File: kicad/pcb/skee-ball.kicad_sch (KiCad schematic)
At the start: 79 parts, among them J1 SPEAKER_P, J10 NHD_RW, J11 NHD_DB1, J12 NHD_DB0, J13 US_ECHO0, J14 US_ECHO1, J15 US_ECHO2, J16 US_ECHO3, J17 US_ECHO4, J18 US_TRIG0_5, J19 US_TRIG1_5, J2 SPEAKER_N, J20 US_TRIG2_5, J21 US_TRIG3_5, J22 US_TRIG4_5, J23 NHD_E1, J24 NHD_E2, J25 ADC_IN1, J26 PWM_SERVO_6, J27 PWM_DC (TIM17_CH1), J28 +24V, J29 NHD_V0, J3 NHD_DB7, J30 BUTTON_P, J31 BUTTON_N, J32 GND, J33 HEADER_GND, J34 HEADER_SWDIO, J35 HEADER_SWCLK, J4 NHD_DB6, J5 NHD_DB5, J6 NHD_DB4, J7 NHD_DB3, J8 NHD_DB2, J9 NHD_RS, U1 D24V22F6, U10 LD1117S33TR_SOT223, U11 LD1117S33TR_SOT223, U12 LD1117S33TR_SOT223, U13 LD1117S33TR_SOT223, U14 LD1117S33TR_SOT223, U2 MAX98357A, U3 D24V22F5, U4 STM32F091RCTx, U5 74HC595, U6 74HC595, U7 74LS08, U8 LD1117S33TR_SOT223, U9 LD1117S33TR_SOT223

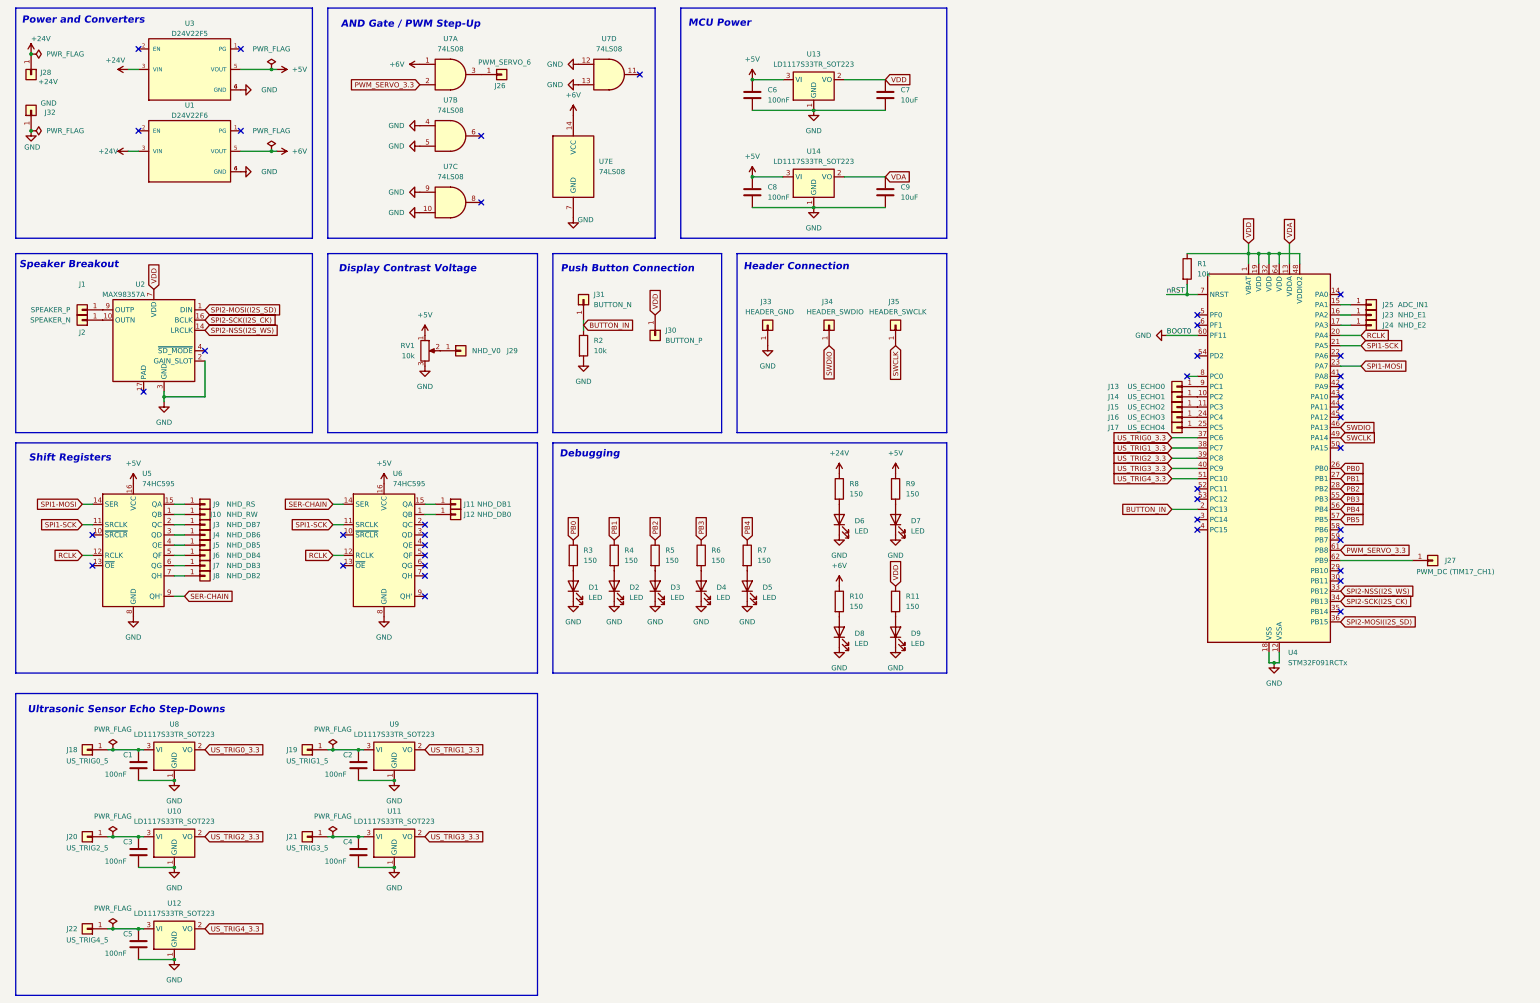
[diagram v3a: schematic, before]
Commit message: added pcb layout
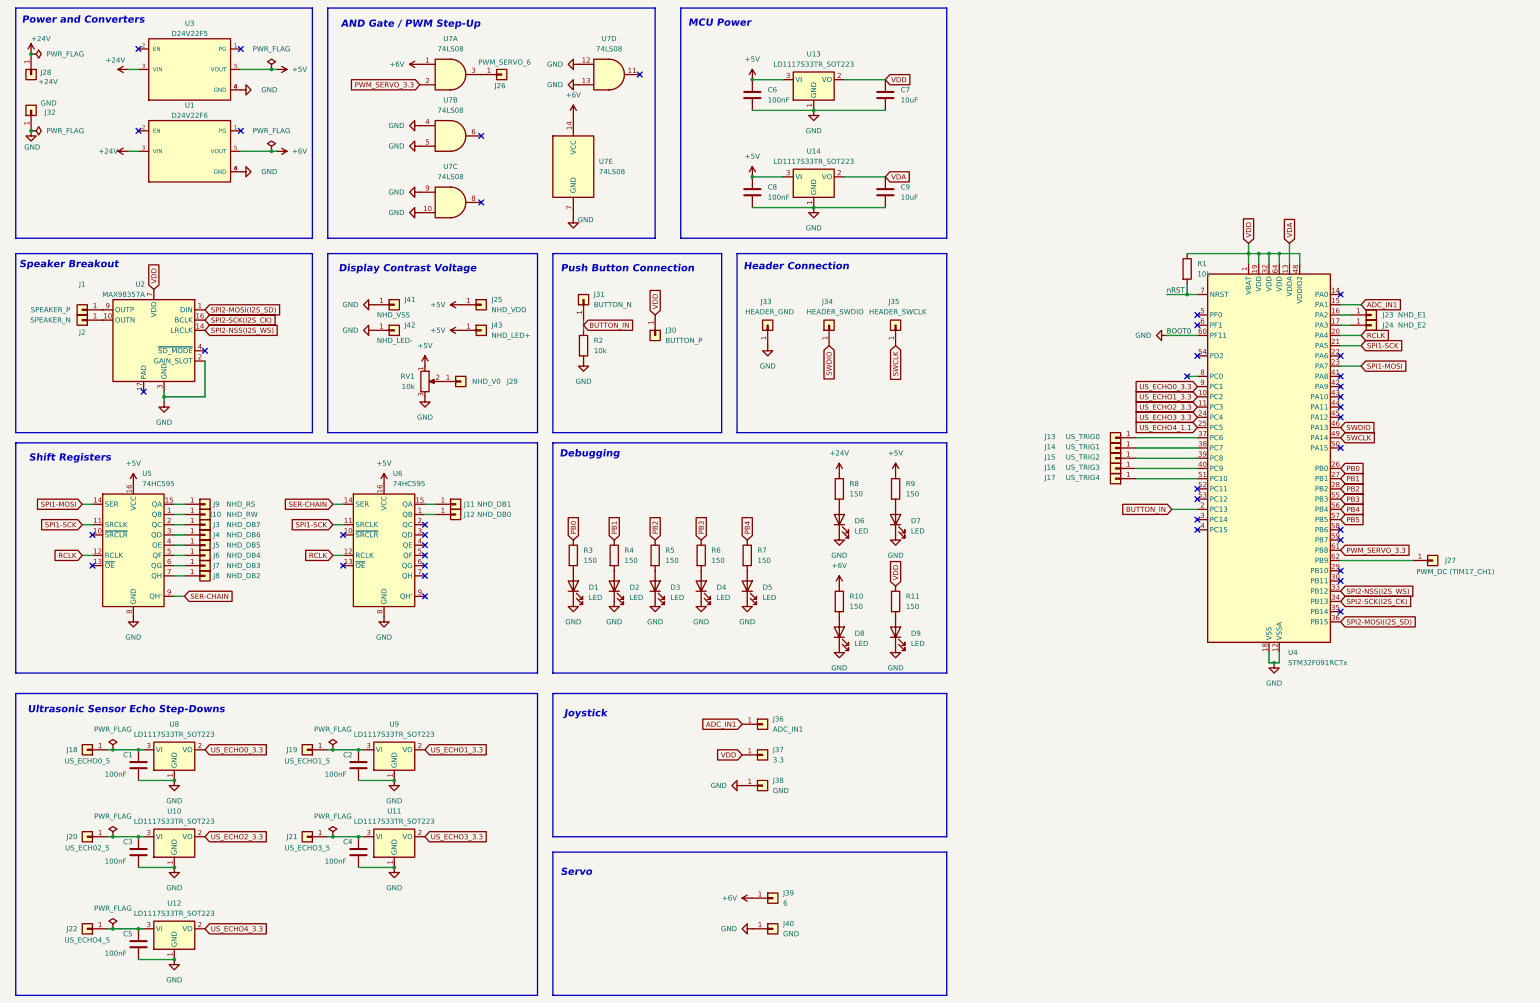
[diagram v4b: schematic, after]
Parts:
- added J36: ADC_IN1, Connector_PinHeader_1.00mm:PinHeader_1x01_P1.00mm_Vertical, symbol Connector_Generic:Conn_01x01
- added J37: 3.3, Connector_PinHeader_1.00mm:PinHeader_1x01_P1.00mm_Vertical, symbol Connector_Generic:Conn_01x01
- added J38, J40: GND, Connector_PinHeader_1.00mm:PinHeader_1x01_P1.00mm_Vertical, symbol Connector_Generic:Conn_01x01
- added J39: 6, Connector_PinHeader_1.00mm:PinHeader_1x01_P1.00mm_Vertical, symbol Connector_Generic:Conn_01x01
- added J41: NHD_VSS, Connector_PinHeader_1.00mm:PinHeader_1x01_P1.00mm_Vertical, symbol Connector_Generic:Conn_01x01
- added J42: NHD_LED-, Connector_PinHeader_1.00mm:PinHeader_1x01_P1.00mm_Vertical, symbol Connector_Generic:Conn_01x01
- added J43: NHD_LED+, Connector_PinHeader_1.00mm:PinHeader_1x01_P1.00mm_Vertical, symbol Connector_Generic:Conn_01x01
- C1, C2, C3, C4, C5, C6, C8: footprint (none) -> Capacitor_SMD:CP_Elec_3x5.3
- C7, C9: footprint (none) -> Capacitor_SMD:CP_Elec_3x5.4
- D1, D2, D3, D4, D5, D6, D7, D8, D9: footprint (none) -> LED_SMD:LED_0201_0603Metric
- J1, J10, J11, J12, J2, J23, J24, J26, J27, J29, J3, J30, J31, J33, J34, J35, J4, J5, J6, J7, J8, J9: footprint (none) -> Connector_PinHeader_1.00mm:PinHeader_1x01_P1.00mm_Vertical
- J13: value US_ECHO0 -> US_TRIG0; footprint (none) -> Connector_PinHeader_1.00mm:PinHeader_1x01_P1.00mm_Vertical
- J14: value US_ECHO1 -> US_TRIG1; footprint (none) -> Connector_PinHeader_1.00mm:PinHeader_1x01_P1.00mm_Vertical
- J15: value US_ECHO2 -> US_TRIG2; footprint (none) -> Connector_PinHeader_1.00mm:PinHeader_1x01_P1.00mm_Vertical
- J16: value US_ECHO3 -> US_TRIG3; footprint (none) -> Connector_PinHeader_1.00mm:PinHeader_1x01_P1.00mm_Vertical
- J17: value US_ECHO4 -> US_TRIG4; footprint (none) -> Connector_PinHeader_1.00mm:PinHeader_1x01_P1.00mm_Vertical
- J18: value US_TRIG0_5 -> US_ECHO0_5; footprint (none) -> Connector_PinHeader_1.00mm:PinHeader_1x01_P1.00mm_Vertical
- J19: value US_TRIG1_5 -> US_ECHO1_5; footprint (none) -> Connector_PinHeader_1.00mm:PinHeader_1x01_P1.00mm_Vertical
- J20: value US_TRIG2_5 -> US_ECH02_5; footprint (none) -> Connector_PinHeader_1.00mm:PinHeader_1x01_P1.00mm_Vertical
- J21: value US_TRIG3_5 -> US_ECHO3_5; footprint (none) -> Connector_PinHeader_1.00mm:PinHeader_1x01_P1.00mm_Vertical
- J22: value US_TRIG4_5 -> US_ECHO4_5; footprint (none) -> Connector_PinHeader_1.00mm:PinHeader_1x01_P1.00mm_Vertical
- J25: value ADC_IN1 -> NHD_VDD; footprint (none) -> Connector_PinHeader_1.00mm:PinHeader_1x01_P1.00mm_Vertical
- J28: footprint (none) -> Connector:Banana_Cliff_FCR7350R_S16N-PC_Horizontal
- J32: footprint (none) -> Connector:Banana_Cliff_FCR7350B_S16N-PC_Horizontal
- R1, R10, R11, R2, R3, R4, R5, R6, R7, R8, R9, RV1: footprint (none) -> Resistor_SMD:R_0201_0603Metric
- U5, U6, U7: footprint (none) -> Package_SO:SSOP-16_5.3x6.2mm_P0.65mm
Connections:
- net +5V: now also J25.1 (Pin_1), J43.1 (Pin_1)
- net +6V: now also J39.1 (Pin_1)
- net GND: now also J38.1 (Pin_1), J40.1 (Pin_1), J41.1 (Pin_1), J42.1 (Pin_1)
- net VDD: now also J37.1 (Pin_1)
- net at J17.1 (Pin_1): now also U4.51 (PC10); no longer U4.25 (PC5)
- net at J14.1 (Pin_1): now also U4.38 (PC7); no longer U4.10 (PC2)
- net at J15.1 (Pin_1): now also U4.39 (PC8); no longer U4.11 (PC3)
- net ADC_IN1: now reaches U4.15 (PA1)
- net ADC_IN1: now also J36.1 (Pin_1); no longer J25.1 (Pin_1)
- net at J16.1 (Pin_1): now also U4.40 (PC9); no longer U4.24 (PC4)
- net at J13.1 (Pin_1): now also U4.37 (PC6); no longer U4.9 (PC1)
- net US_TRIG0_3.3 renamed US_ECHO0_3.3
- net US_ECHO0_3.3: now also U4.9 (PC1); no longer U4.37 (PC6)
- net US_TRIG1_3.3 renamed US_ECHO1_3.3
- net US_ECHO1_3.3: now also U4.10 (PC2); no longer U4.38 (PC7)
- net US_TRIG2_3.3 renamed US_ECHO2_3.3
- net US_ECHO2_3.3: now also U4.11 (PC3); no longer U4.39 (PC8)
- net US_TRIG3_3.3 renamed US_ECHO3_3.3
- net US_ECHO3_3.3: now also U4.24 (PC4); no longer U4.40 (PC9)
- net US_TRIG4_3.3 renamed US_ECHO4_3.3
- net US_ECHO4_3.3: no longer U4.51 (PC10)
- new net US_ECHO4_1.1: U4.25 (PC5)
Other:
- note added: "Joystick"
- note added: "Servo"
- moved on the sheet: J29, RV1

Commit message: begin routing on pcb
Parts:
- C1, C2, C3, C4, C5, C6, C8: footprint Capacitor_SMD:CP_Elec_3x5.3 -> Capacitor_SMD:C_0805_2012Metric_Pad1.18x1.45mm_HandSolder
- C7, C9: footprint Capacitor_SMD:CP_Elec_3x5.4 -> Capacitor_SMD:C_0805_2012Metric_Pad1.18x1.45mm_HandSolder
- J1, J10, J11, J12, J13, J14, J15, J16, J17, J18, J19, J2, J20, J21, J22, J23, J24, J25, J26, J27, J29, J3, J30, J31, J33, J34, J35, J36, J37, J38, J39, J4, J40, J41, J42, J43, J5, J6, J7, J8, J9: footprint Connector_PinHeader_1.00mm:PinHeader_1x01_P1.00mm_Vertical -> Connector_PinHeader_2.54mm:PinHeader_1x01_P2.54mm_Vertical
- R1, R10, R11, R2, R3, R4, R5, R6, R7, R8, R9: footprint Resistor_SMD:R_0201_0603Metric -> Resistor_SMD:R_0805_2012Metric_Pad1.20x1.40mm_HandSolder
- RV1: footprint Resistor_SMD:R_0201_0603Metric -> Potentiometer_THT:Potentiometer_Bourns_3339P_Vertical

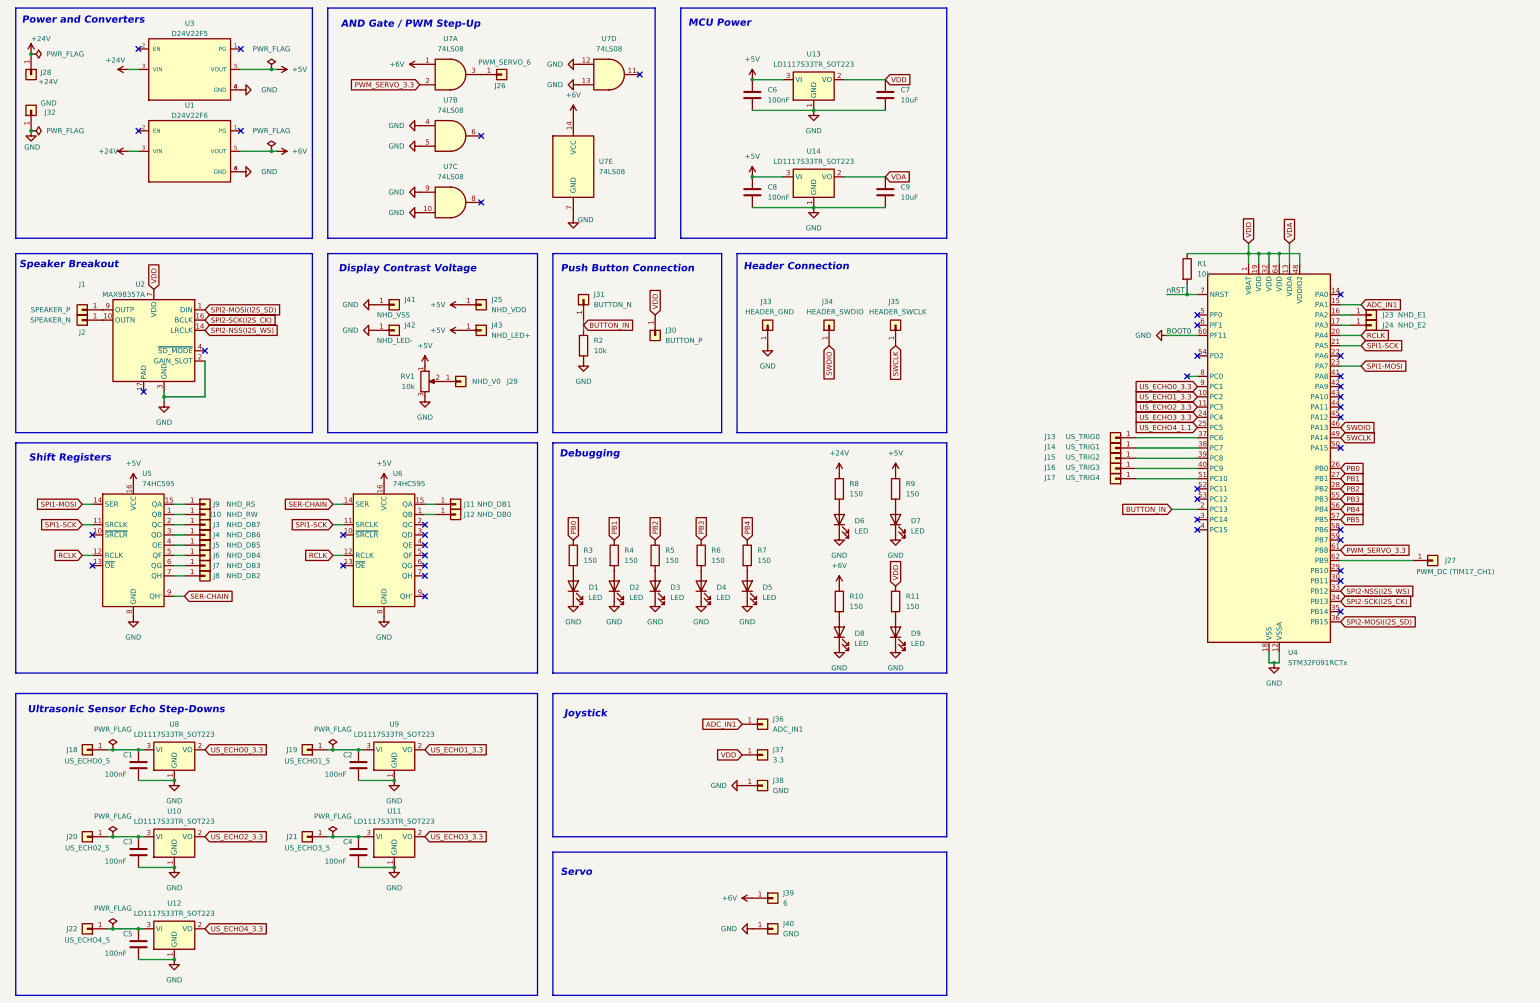
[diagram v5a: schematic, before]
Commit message: add decoupling circuitry for mcu power
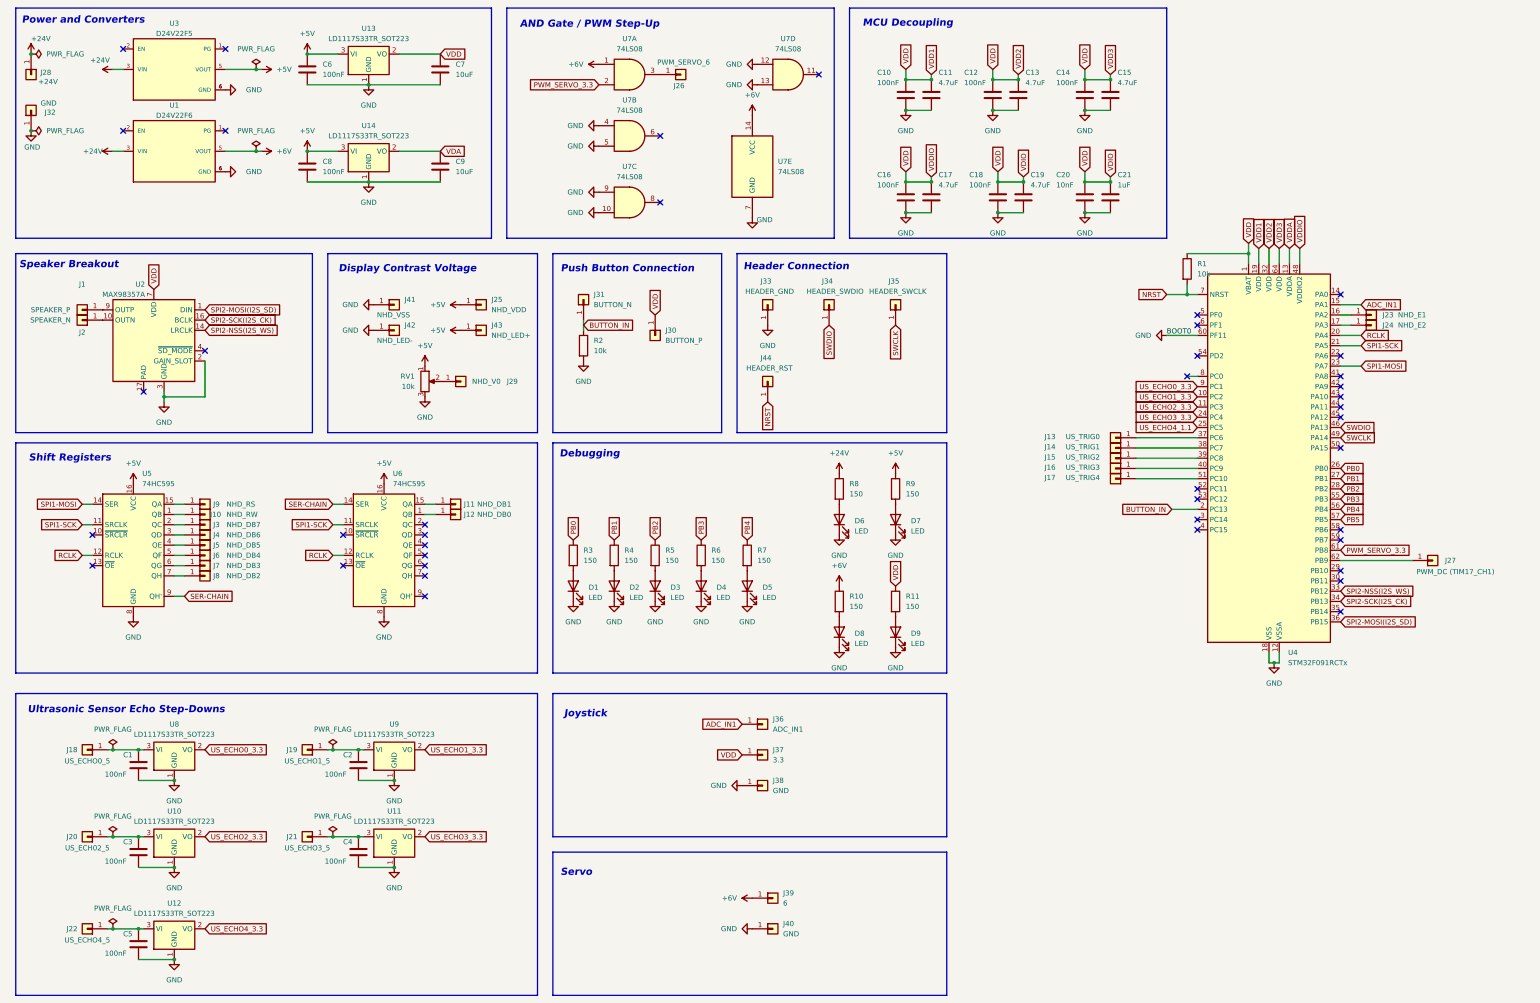
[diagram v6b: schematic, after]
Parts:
- added C10, C12, C14, C16, C18: 100nF, Capacitor_SMD:C_0805_2012Metric_Pad1.18x1.45mm_HandSolder, symbol Device:C
- added C11, C13, C15, C17, C19: 4.7uF, Capacitor_SMD:C_0805_2012Metric_Pad1.18x1.45mm_HandSolder, symbol Device:C
- added C20: 10nF, Capacitor_SMD:C_0805_2012Metric_Pad1.18x1.45mm_HandSolder, symbol Device:C
- added C21: 1uF, Capacitor_SMD:C_0805_2012Metric_Pad1.18x1.45mm_HandSolder, symbol Device:C
- added J44: HEADER_RST, Connector_PinHeader_2.54mm:PinHeader_1x01_P2.54mm_Vertical, symbol Connector_Generic:Conn_01x01
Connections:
- net GND: now also C10.2, C11.2, C12.2, C13.2, C14.2, C15.2, C16.2, C17.2, C18.2, C19.2, C20.2, C21.2
- net VDA: no longer U4.13 (VDDA)
- net VDD: now also C10.1, C11.1, C12.1, C13.1, C14.1, C15.1, C16.1, C17.1, C18.1, C19.1, C20.1, C21.1
- net nRST renamed NRST
- net NRST: now also J44.1 (Pin_1)
- new net VDDA: U4.13 (VDDA)
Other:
- note added: "MCU Decoupling"
- note removed: "MCU Power"
- moved on the sheet: C6, C7, C8, C9, J26, J33, J34, J35, U1, U13, U14, U3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
